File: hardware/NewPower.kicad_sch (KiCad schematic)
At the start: 19 parts

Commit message: some changes
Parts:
- removed C? (x2): C, symbol rlib_passive:C
- removed L?: L, symbol rlib_passive:L
- added C28: C, symbol rlib_passive:C
- added D2: HCTL HC-1.25-3PWT, rlib_connectors:CONN-SMD_HC-1.25-3PWT, symbol rlib_connectors:HCTL HC-1.25-3PWT
- L10, L11, L12, L13: renamed from L?; footprint (none) -> rlib_passive:INDC2520X120N
- gave numbers to parts that had none: 12
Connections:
- net +1V1: no longer U9.15 (VFB2)
- net GND: now also C28.2
- net VCC: no longer U9.13 (VCC2)
- net at U9.21 (LDO3): now also C28.1
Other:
- moved on the sheet: C23, C24, C25, C26, C27, C29, C30, C32, C33, L10, L11, L12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

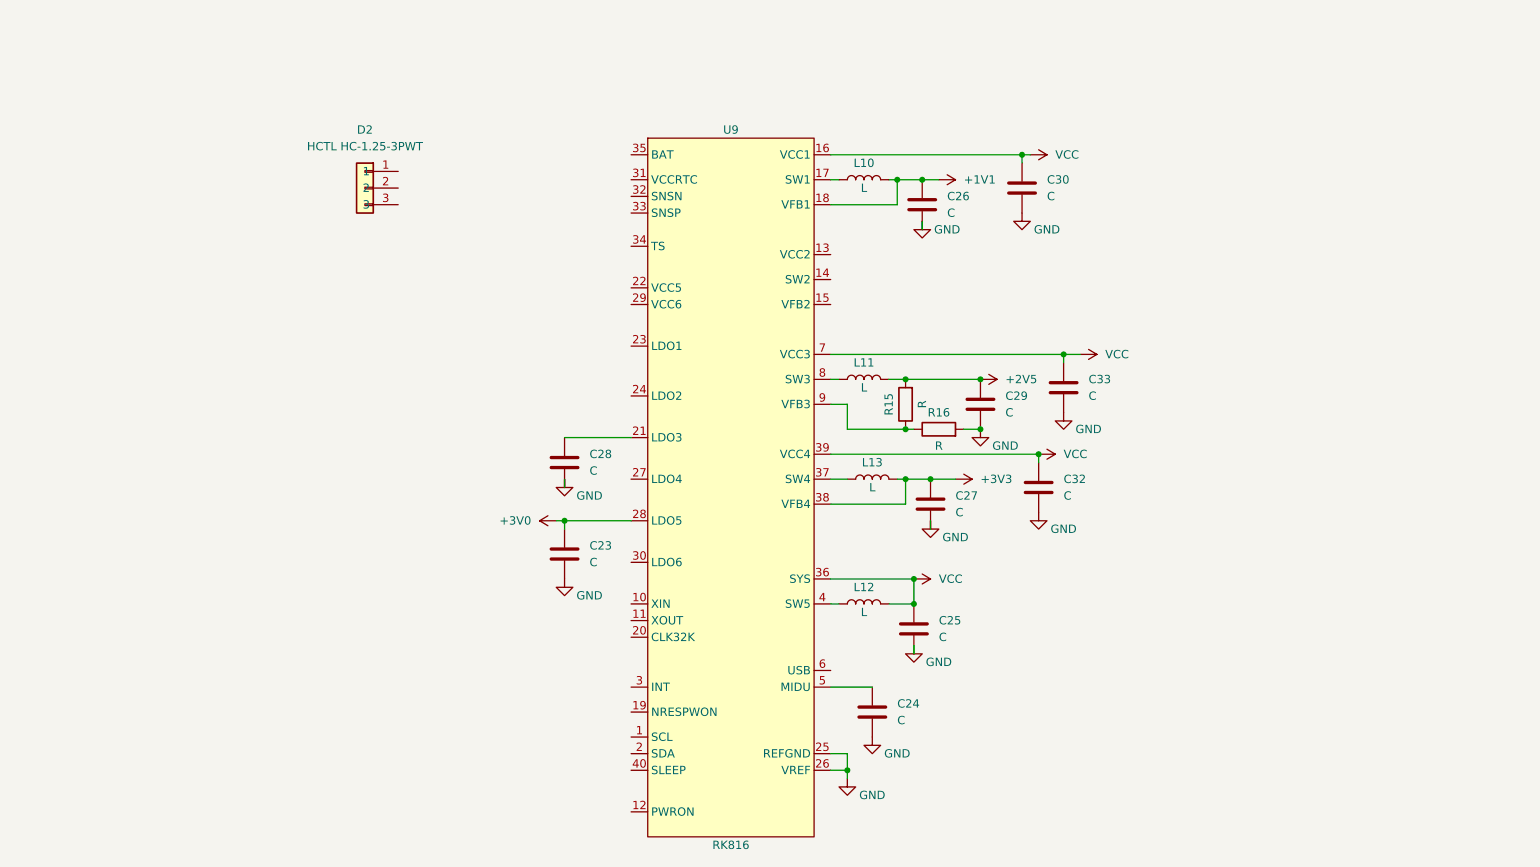
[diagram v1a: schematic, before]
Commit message: new power list added
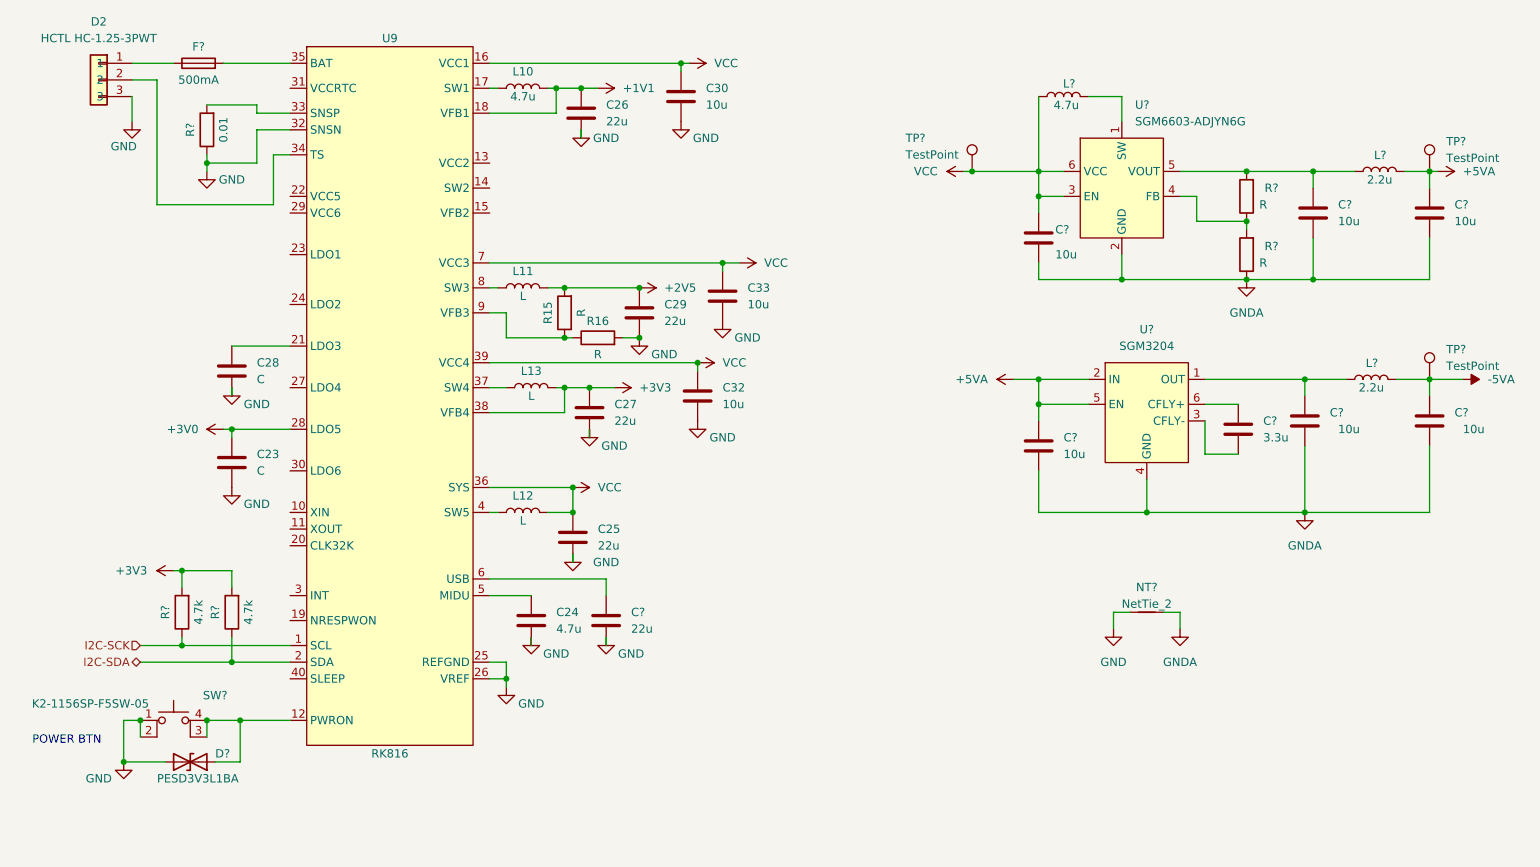
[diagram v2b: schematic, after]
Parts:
- added C? (x6): 10u, symbol rlib_passive:C
- added C?: 3.3u, symbol rlib_passive:C
- added C?: 22u, symbol rlib_passive:C
- added D?: PESD3V3L1BA, rlib_passive:D_SOD-323F, symbol rlib_passive:PESD3V3L1BA
- added F?: 500mA, rlib_passive:FUSC3216X85N, symbol rlib_passive:Fuse
- added L?: 4.7u, rlib_passive:IND_LQH32PN4R7NN0L, symbol rlib_passive:L
- added L? (x2): 2.2u, rlib_passive:IND_LQH32PN4R7NN0L, symbol rlib_passive:L
- added NT?: NetTie_2, symbol Device:NetTie_2
- added R?: 0.01, symbol Device:R
- added R? (x2): 4.7k, symbol Device:R
- added R? (x2): R, symbol Device:R
- added SW?: K2-1156SP-F5SW-05, rlib_buttons:K2-1156SP-F5SW-05, symbol rlib_buttons:K2-1156SP-F5SW-05
- added TP? (x3): TestPoint, symbol Connector:TestPoint
- added U?: SGM6603-ADJYN6G, rlib_power:SOT-23-6, symbol rlib_power:SGM6603-ADJYN6G
- added U?: SGM3204, rlib_power:SOT-23-6, symbol rlib_power:SGM3204
- C24: value C -> 4.7u
- C25, C26, C27, C29: value C -> 22u
- C30, C32, C33: value C -> 10u
- L10: value L -> 4.7u; footprint rlib_passive:INDC2520X120N -> rlib_passive:IND_LQH32PN4R7NN0L
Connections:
- net +3V3: now also R?.2, R?.2
- net GND: now also D2.3, U9.32 (SNSN), C?.2, D?.2 (A2), NT?.1, R?.1, SW?.1, SW?.2
- net VCC: now also C?.1, L?.1, TP?.1, U?.3 (EN), U?.6 (VCC)
- net at D2.1: now also F?.1
- net at D2.2: now also U9.34 (TS)
- net I2C-SCK: now reaches U9.1 (SCL)
- net I2C-SCK: now also R?.1
- net at U9.12 (PWRON): now also D?.1 (A1), SW?.3 (K), SW?.4 (A)
- net I2C-SDA: now reaches U9.2 (SDA)
- net I2C-SDA: now also R?.1
- net at U9.33 (SNSP): now also R?.2
- net at U9.35 (BAT): now also F?.2
- net at U9.6 (USB): now also C?.1
- new net: C?.1, U?.6 (CFLY+)
- new net: C?.2, U?.3 (CFLY-)
- new net: L?.2, U?.1 (SW)
- new net: C?.1, L?.1, U?.1 (OUT)
- new net: C?.1, L?.1, R?.2, U?.5 (VOUT)
- new net: R?.1, R?.2, U?.4 (FB)
- new net +5VA: C?.1, C?.1, L?.2, TP?.1, U?.2 (IN), U?.5 (EN)
- new net -5VA: C?.1, L?.2, TP?.1
- new net GNDA: C?.2, C?.2, C?.2, C?.2, C?.2, C?.2, NT?.2, R?.1, U?.2 (GND), U?.4 (GND)
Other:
- note added: "POWER BTN"
- moved on the sheet: C23, C24, C25, C26, C27, C28, C29, C30, C32, C33, D2, L10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
